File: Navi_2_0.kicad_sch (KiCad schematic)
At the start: 107 parts, among them J1 USB_B_Micro, J10 BAT-, J2 Conn_01x24_Male, J27 Micro_SD_Card_Det, J8 SELECT, J9 BAT+, Q1 DMG2301L-7, Q2 TF2310, Q3 DMG2301L-7, Q4 Q_NPN_BEC, Q5 Q_NPN_BEC, Q6 DMG2301L-7, Q7 DMG2301L-7, SW1 SW_Push, U1 MT3420C, U2 MT3420C, U3 ESP32-WROOM-32, U4 CH340K, U5 L96-M33, U6 LSM6DS3, U7 TCN75-3.3

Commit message: Zwischenstand erste Platzierung
Es fehlen noch die Schaltregler und Reset / Programmierschaltung
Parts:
- Q4, Q5: footprint (none) -> Package_TO_SOT_SMD:SOT-23
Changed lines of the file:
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@@
       (effects (font (size 1.27 1.27)) (justify left))
     )
-    (property "Footprint" "" (id 2) (at 127 113.03 0)
+    (property "Footprint" "Package_TO_SOT_SMD:SOT-23" (id 2) (at 127 113.03 0)
       (effects (font (size 1.27 1.27)) hide)
     )
@@
       (effects (font (size 1.27 1.27)) (justify left))
     )
-    (property "Footprint" "" (id 2) (at 129.54 92.71 0)
+    (property "Footprint" "Package_TO_SOT_SMD:SOT-23" (id 2) (at 129.54 92.71 0)
       (effects (font (size 1.27 1.27)) hide)
     )
@@
     )
     (path "/f565b841-9b2c-4ec1-9ce9-08480c454181"
-      (reference "Q4") (unit 1) (value "Q_NPN_BEC") (footprint "")
+      (reference "Q4") (unit 1) (value "Q_NPN_BEC") (footprint "Package_TO_SOT_SMD:SOT-23")
     )
     (path "/d0cfeb97-bcb6-465d-a0b7-4c1fdce848f8"
-      (reference "Q5") (unit 1) (value "Q_NPN_BEC") (footprint "")
+      (reference "Q5") (unit 1) (value "Q_NPN_BEC") (footprint "Package_TO_SOT_SMD:SOT-23")
     )
     (path "/00000000-0000-0000-0000-00005fd75a6e"

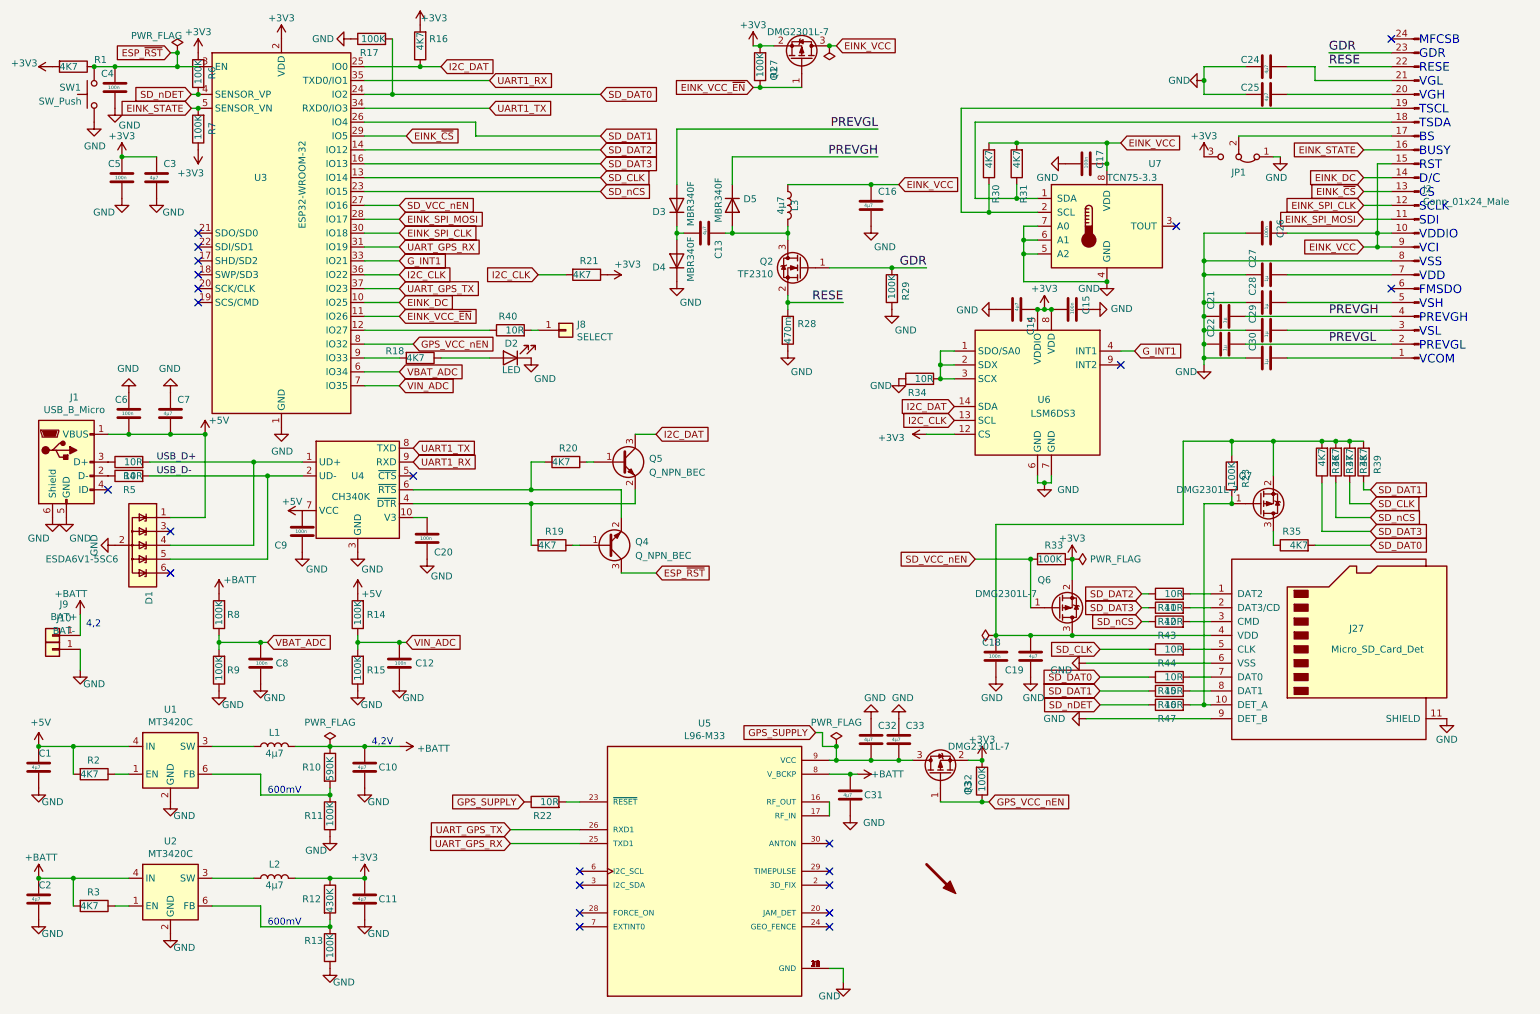
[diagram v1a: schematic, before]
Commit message: Update G-Sensor
#9 Ersetzt mit lsm303ah
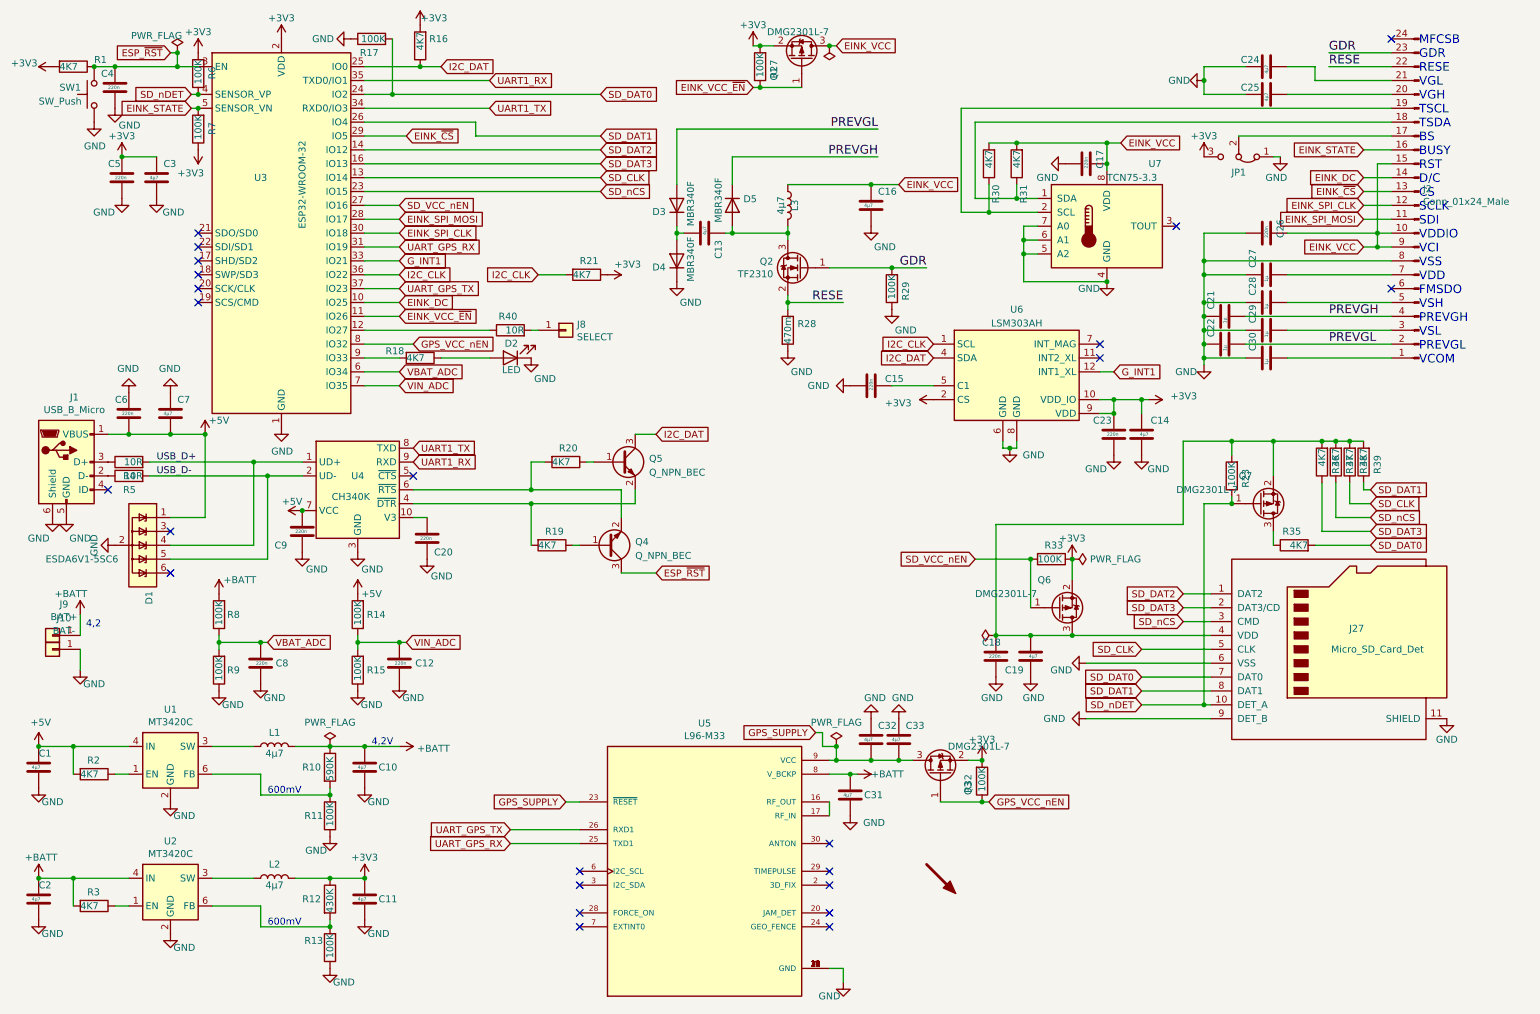
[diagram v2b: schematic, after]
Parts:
- removed R22, R34, R41, R42, R43, R44, R45, R46, R47: 10R, Resistor_SMD:R_0603_1608Metric, symbol Device:R
- removed U6: LSM6DS3, Package_LGA:LGA-14_3x2.5mm_P0.5mm_LayoutBorder3x4y, symbol Sensor_Motion:LSM6DS3
- added C23: 220n, Capacitor_SMD:C_0603_1608Metric, symbol Device:C
- added U6: LSM303AH, Package_LGA:LGA-12_2x2mm_P0.5mm, symbol TheBrutzlers_Lib:LSM303AH
- C12, C15, C17, C18, C20, C26, C4, C5, C6, C8, C9: value 100n -> 220n; LCSC C478888 -> C163696
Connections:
- net +3V3: now also C14.2, C23.1, U6.10 (VDD_IO), U6.2 (CS), U6.9 (VDD); no longer C14.1, C15.2
- net GND: now also C14.1, C15.2, C23.2, U6.6 (GND), U6.8 (GND); no longer C14.2, C15.1
- net GPS_SUPPLY: now also U5.23 (~RESET)
- net G_INT1: now also U6.12 (INT1_XL)
- net I2C_CLK: now also U6.1 (SCL)
- net I2C_DAT: now also U6.4 (SDA)
- net SD_CLK: now also J27.5 (CLK)
- net SD_DAT0: now also J27.7 (DAT0)
- net SD_DAT1: now also J27.8 (DAT1)
- net SD_DAT2: now also J27.1 (DAT2)
- net SD_DAT3: now also J27.2 (DAT3/CD)
- net SD_nCS: now also J27.3 (CMD)
- net SD_nDET: now also J27.10 (DET_A), Q7.1 (G), R23.1
- new net: C15.1, U6.5 (C1)
- no-connect marks 23 -> 24
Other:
- moved on the sheet: C14

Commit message: Commit vor Routing
Sicherheitscommit vor routing
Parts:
- removed J8: SELECT, TestPoint:TestPoint_Pad_D1.0mm, symbol Connector_Generic:Conn_01x01
- removed R40: 10R, Resistor_SMD:R_0603_1608Metric, symbol Device:R
- added SW2: SW_Push, Button_Switch_SMD:SW_DIP_SPSTx01_Slide_Copal_CHS-01B_W7.62mm_P1.27mm, symbol Switch:SW_Push
- SW1: footprint Navi_2_0:TS36CA -> Button_Switch_SMD:SW_DIP_SPSTx01_Slide_Copal_CHS-01B_W7.62mm_P1.27mm
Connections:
- net GND: now also SW2.2
- net at U3.12 (IO27): now also SW2.1
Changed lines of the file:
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@@
     (stroke (width 0) (type solid) (color 0 0 0 0))
   )
-  (wire (pts (xy 77.47 71.12) (xy 100.33 71.12))
+  (wire (pts (xy 77.47 71.12) (xy 101.6 71.12))
     (stroke (width 0) (type solid) (color 0 0 0 0))
   )
@@
     (stroke (width 0) (type solid) (color 0 0 0 0))
   )
-  (wire (pts (xy 107.95 71.12) (xy 109.22 71.12))
-    (stroke (width 0) (type solid) (color 0 0 0 0))
-  )
   (wire (pts (xy 107.95 95.25) (xy 110.49 95.25))
     (stroke (width 0) (type solid) (color 0 0 0 0))
@@
     (pin "1")
   )
+  (symbol (lib_id "power:GND") (at 111.76 71.12 90) (unit 1)
+    (in_bom yes) (on_board yes)
+    (property "Reference" "#PWR018" (id 0) (at 118.11 71.12 0)
+      (effects (font (size 1.27 1.27)) hide)
+    )
+    (property "Value" "GND" (id 1) (at 115.57 68.58 0))
+    (property "Footprint" "" (id 2) (at 111.76 71.12 0)
+      (effects (font (size 1.27 1.27)) hide)
+    )
+    (property "Datasheet" "" (id 3) (at 111.76 71.12 0)
+      (effects (font (size 1.27 1.27)) hide)
+    )
+    (pin "1")
+  )
   (symbol (lib_id "power:GND") (at 134.62 62.23 0) (unit 1)
     (in_bom yes) (on_board yes)
@@
     (pin "1")
   )
-  (symbol (lib_id "Connector_Generic:Conn_01x01") (at 114.3 71.12 0) (unit 1)
-    (in_bom yes) (on_board yes)
-    (property "Reference" "J8" (id 0) (at 116.332 70.0532 0)
-      (effects (font (size 1.27 1.27)) (justify left))
-    )
-    (property "Value" "SELECT" (id 1) (at 116.332 72.3646 0)
-      (effects (font (size 1.27 1.27)) (justify left))
-    )
-    (property "Footprint" "TestPoint:TestPoint_Pad_D1.0mm" (id 2) (at 114.3 71.12 0)
-      (effects (font (size 1.27 1.27)) hide)
-    )
-    (property "Datasheet" "~" (id 3) (at 114.3 71.12 0)
-      (effects (font (size 1.27 1.27)) hide)
-    )
-    (pin "1")
-  )
   (symbol (lib_id "Device:R") (at 24.13 22.86 270) (unit 1)
     (in_bom yes) (on_board yes)
@@
     (pin "2")
   )
-  (symbol (lib_id "Device:R") (at 104.14 71.12 90) (unit 1)
-    (in_bom yes) (on_board yes)
-    (property "Reference" "R40" (id 0) (at 105.41 68.58 90)
-      (effects (font (size 1.27 1.27)) (justify left))
-    )
-    (property "Value" "10R" (id 1) (at 106.68 71.12 90)
-      (effects (font (size 1.27 1.27)) (justify left))
-    )
-    (property "Footprint" "Resistor_SMD:R_0603_1608Metric" (id 2) (at 104.14 72.898 90)
-      (effects (font (size 1.27 1.27)) hide)
-    )
-    (property "Datasheet" "" (id 3) (at 104.14 71.12 0)
-      (effects (font (size 1.27 1.27)) hide)
-    )
-    (property "LCSC" "C217691" (id 4) (at 104.14 71.12 90)
-      (effects (font (size 1.27 1.27)) hide)
-    )
-    (pin "1")
-    (pin "2")
-  )
   (symbol (lib_id "Device:R") (at 111.76 110.49 270) (unit 1)
     (in_bom yes) (on_board yes)
@@
   (symbol (lib_id "Device:C") (at 193.04 130.81 0) (unit 1)
     (in_bom yes) (on_board yes)
-    (property "Reference" "C18" (id 0) (at 190.5 128.27 0)
+    (property "Reference" "C18" (id 0) (at 189.23 133.35 0)
       (effects (font (size 1.27 1.27)) (justify left))
     )
@@
   (symbol (lib_id "Device:C") (at 199.39 130.81 180) (unit 1)
     (in_bom yes) (on_board yes)
-    (property "Reference" "C19" (id 0) (at 198.12 133.35 0)
+    (property "Reference" "C19" (id 0) (at 199.39 133.35 0)
       (effects (font (size 1.27 1.27)) (justify left))
     )
@@
       (effects (font (size 1.27 1.27)) (justify right))
     )
-    (property "Footprint" "Navi_2_0:TS36CA" (id 2) (at 22.86 27.94 0)
+    (property "Footprint" "Button_Switch_SMD:SW_DIP_SPSTx01_Slide_Copal_CHS-01B_W7.62mm_P1.27mm" (id 2) (at 22.86 27.94 0)
       (effects (font (size 1.27 1.27)) hide)
     )
@@
     (pin "2")
   )
+  (symbol (lib_id "Switch:SW_Push") (at 106.68 71.12 0) (unit 1)
+    (in_bom yes) (on_board yes) (fields_autoplaced)
+    (property "Reference" "SW2" (id 0) (at 106.68 64.77 0))
+    (property "Value" "SW_Push" (id 1) (at 106.68 67.31 0))
+    (property "Footprint" "Button_Switch_SMD:SW_DIP_SPSTx01_Slide_Copal_CHS-01B_W7.62mm_P1.27mm" (id 2) (at 106.68 66.04 0)
+      (effects (font (size 1.27 1.27)) hide)
+    )
+    (property "Datasheet" "~" (id 3) (at 106.68 66.04 0)
+      (effects (font (size 1.27 1.27)) hide)
+    )
+    (pin "1")
+    (pin "2")
+  )
   (symbol (lib_id "Jumper:Jumper_3_Bridged12") (at 237.49 39.37 180) (unit 1)
     (in_bom yes) (on_board yes)
@@
       (reference "#PWR017") (unit 1) (value "GND") (footprint "")
     )
+    (path "/be0ae6e6-f0a6-410f-8c68-662f77289e15"
+      (reference "#PWR018") (unit 1) (value "GND") (footprint "")
+    )
     (path "/00000000-0000-0000-0000-00006051b2ed"
       (reference "#PWR019") (unit 1) (value "GND") (footprint "")
@@
       (reference "J2") (unit 1) (value "Conn_01x24_Male") (footprint "Connector_FFC-FPC:Hirose_FH12-24S-0.5SH_1x24-1MP_P0.50mm_Horizontal")
     )
-    (path "/00000000-0000-0000-0000-000060d361e1"
-      (reference "J8") (unit 1) (value "SELECT") (footprint "TestPoint:TestPoint_Pad_D1.0mm")
-    )
     (path "/00000000-0000-0000-0000-0000610ab8b1"
       (reference "J9") (unit 1) (value "BAT+") (footprint "TestPoint:TestPoint_Pad_D3.0mm")
@@
       (reference "R39") (unit 1) (value "4K7") (footprint "Resistor_SMD:R_0603_1608Metric")
     )
-    (path "/00000000-0000-0000-0000-0000605741d8"
-      (reference "R40") (unit 1) (value "10R") (footprint "Resistor_SMD:R_0603_1608Metric")
-    )
     (path "/00000000-0000-0000-0000-000060454bf6"
-      (reference "SW1") (unit 1) (value "SW_Push") (footprint "Navi_2_0:TS36CA")
+      (reference "SW1") (unit 1) (value "SW_Push") (footprint "Button_Switch_SMD:SW_DIP_SPSTx01_Slide_Copal_CHS-01B_W7.62mm_P1.27mm")
+    )
+    (path "/89b92065-825e-400c-8600-fe8d34385717"
+      (reference "SW2") (unit 1) (value "SW_Push") (footprint "Button_Switch_SMD:SW_DIP_SPSTx01_Slide_Copal_CHS-01B_W7.62mm_P1.27mm")
     )
     (path "/00000000-0000-0000-0000-0000602d44e9"
